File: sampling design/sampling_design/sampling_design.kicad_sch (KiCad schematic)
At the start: 32 parts, among them J1 GX Connector Female, J2 GX Connector Male, J3 Microfit Connector Male, J4 Connector Microfit Female, M1 MQ4_Module, T1 TGS2620_Module, T2 TGS2602_Module, T3 TGS2600_Module, T4 TGS5042, U1 LM358, U2 OPA2333AID, U3 ESP32-S3-DEVKITC-1-N8R2

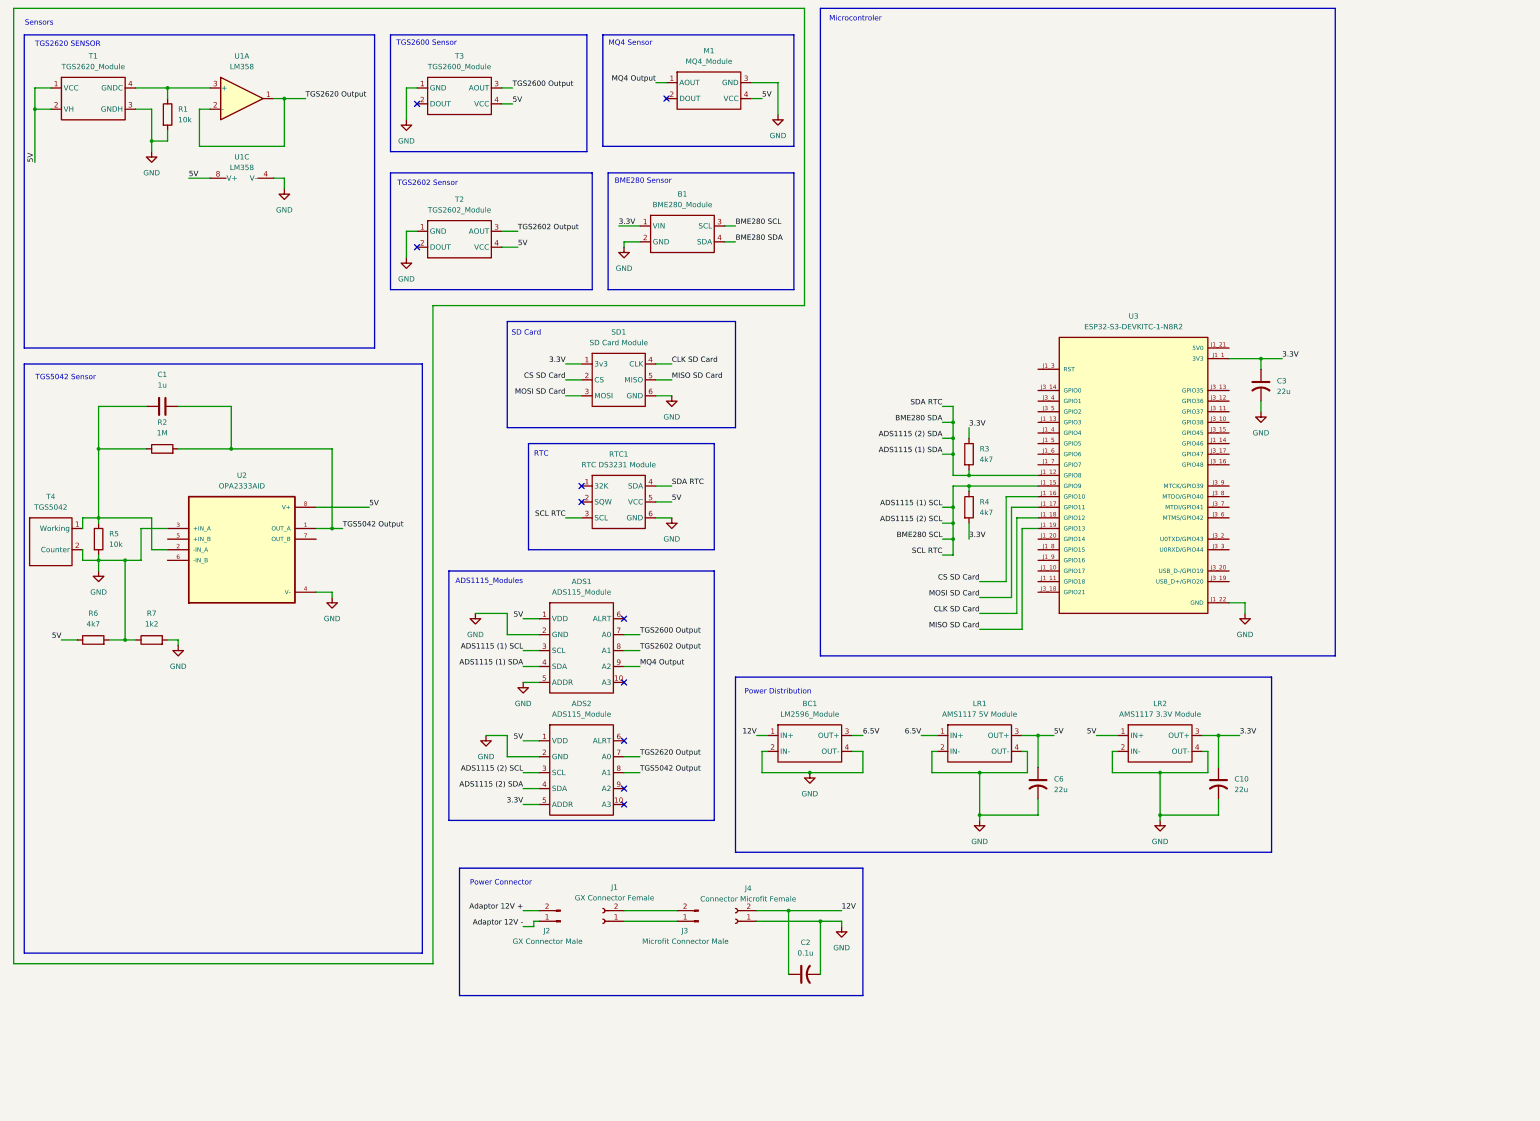
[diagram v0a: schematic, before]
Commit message: update new schematic bcs of tgs2602 unavalaible module
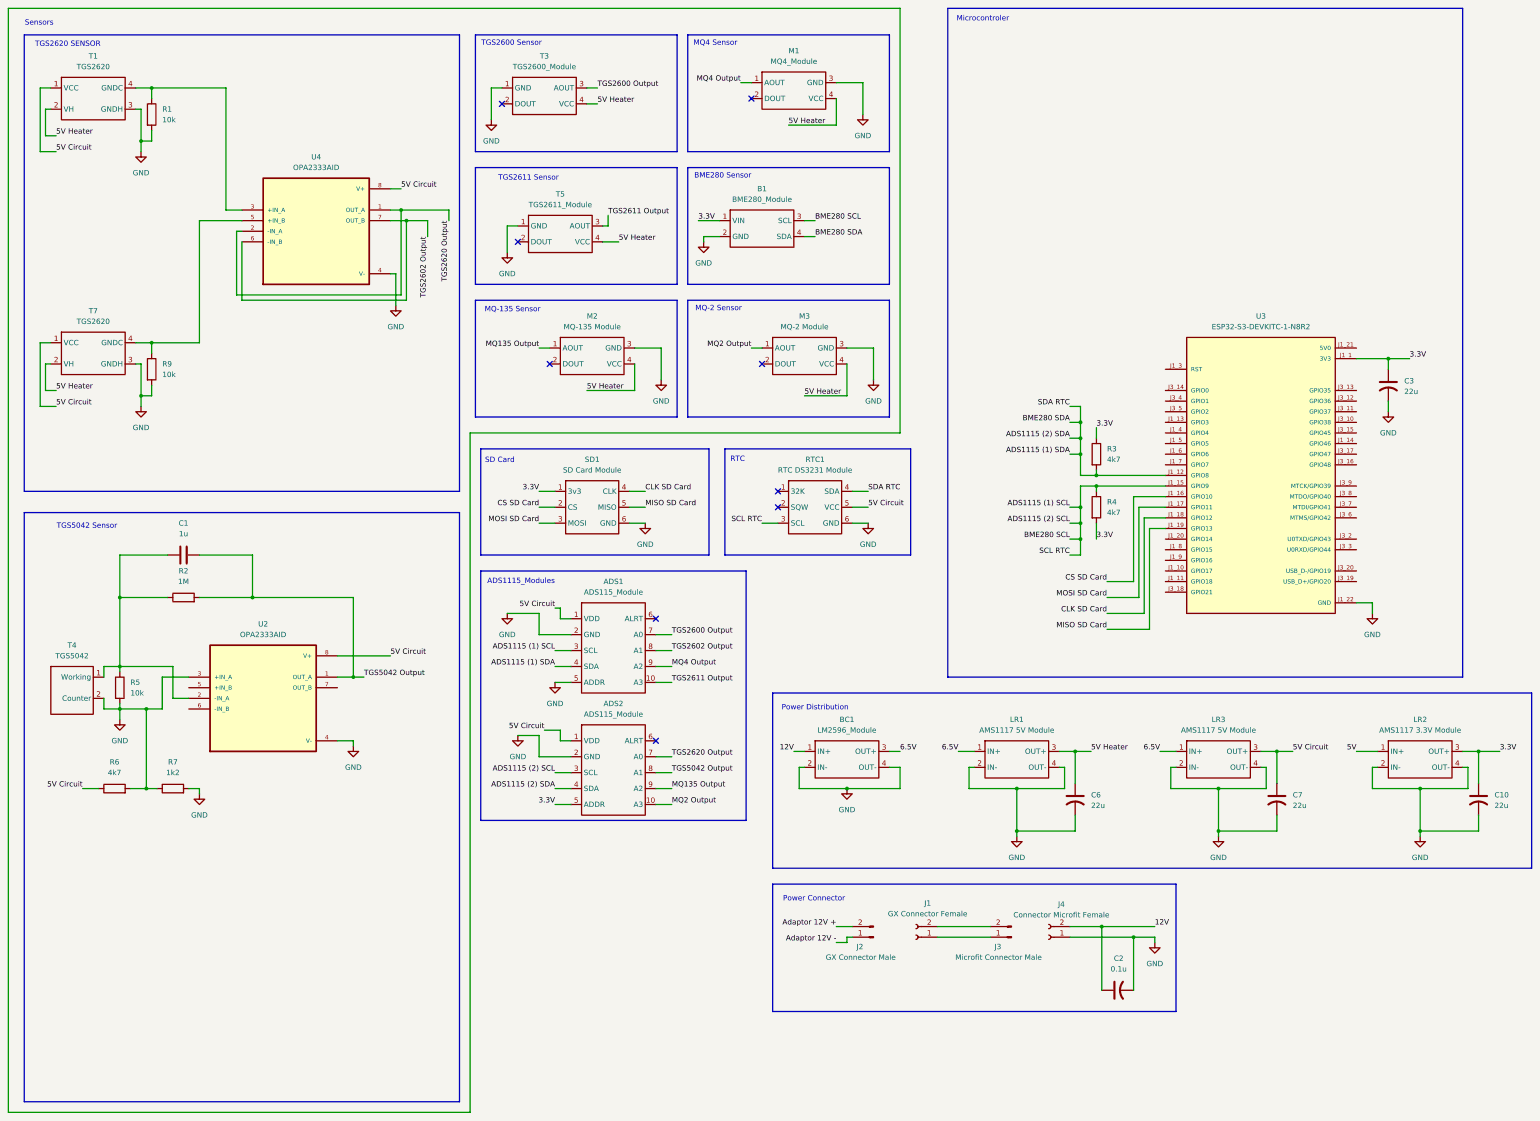
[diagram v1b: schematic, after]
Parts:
- removed T2: TGS2602_Module, symbol TGS_Module:TGS2602
- removed U1: LM358, symbol Amplifier_Operational:LM358
- added C7: 22u, symbol Device:C_US
- added LR3: AMS1117 5V Module, symbol Linear_Voltage_Regulator_Module:AMS1117_5V_Module
- added M2: MQ-135 Module, symbol MQ_Module:MQ-2
- added M3: MQ-2 Module, symbol MQ_Module:MQ-2
- added R9: 10k, symbol Device:R
- added T5: TGS2611_Module, symbol TGS_Module:TGS2611
- added T7: TGS2620, symbol Sensor_Gas:TGS2602
- added U4: OPA2333AID, OPA2333AID:SOIC127P599X175-8N, symbol OPA2333AID:OPA2333AID
- T1: value TGS2620_Module -> TGS2620
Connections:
- net 5V: no longer ADS1.1 (VDD), ADS2.1 (VDD), C6.1, LR1.3 (OUT+), M1.4 (VCC), R6.1, RTC1.5 (VCC), T1.1 (VCC), T1.2 (VH), T3.4 (VCC), U2.8 (V+)
- net 6.5V: now also LR3.1 (IN+)
- net GND: now also C7.2, LR3.2 (IN-), LR3.4 (OUT-), M2.3 (GND), M3.3 (GND), R9.2, T5.1 (GND), T7.3 (GNDH), U4.4 (V-)
- net TGS2602 Output: now also U4.6 (-IN_B), U4.7 (OUT_B)
- net TGS2620 Output: now also U4.1 (OUT_A), U4.2 (-IN_A)
- net MQ2 Output: now reaches ADS2.10 (A3)
- net MQ2 Output: now also M3.1 (AOUT)
- net MQ135 Output: now reaches ADS2.9 (A2)
- net MQ135 Output: now also M2.1 (AOUT)
- net at R1.1, T1.4 (GNDC): now also U4.3 (+IN_A)
- net TGS2611 Output: now reaches ADS1.10 (A3)
- net TGS2611 Output: now also T5.3 (AOUT)
- new net: R9.1, T7.4 (GNDC), U4.5 (+IN_B)
- new net 5V Circuit: ADS1.1 (VDD), ADS2.1 (VDD), C7.1, LR3.3 (OUT+), R6.1, RTC1.5 (VCC), T1.1 (VCC), T7.1 (VCC), U2.8 (V+), U4.8 (V+)
- new net 5V Heater: C6.1, LR1.3 (OUT+), M1.4 (VCC), M2.4 (VCC), M3.4 (VCC), T1.2 (VH), T3.4 (VCC), T5.4 (VCC), T7.2 (VH)
- no-connect marks 10 -> 9
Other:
- note added: "MQ-135 Sensor"
- note added: "MQ-2 Sensor"
- note added: "TGS2611 Sensor"
- note removed: "TGS2602 Sensor"
- moved on the sheet: ADS1, ADS2, B1, BC1, C1, C10, C2, C3, C6, J1, J2, J3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

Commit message: update
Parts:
- removed R3, R4: 4k7, symbol Device:R
- T7: value TGS2620 -> TGS2602
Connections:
- net 3V3: no longer ADS2.5 (ADDR)
- net 5V: now also ADS2.5 (ADDR)
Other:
- note added: "TGS2620 & TGS2602 SENSOR"
- note removed: "TGS2620 SENSOR"
